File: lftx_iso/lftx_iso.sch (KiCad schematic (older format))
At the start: 9 parts, among them P1 CONN_01X02, P2 CONN_02X08, P3 CONN_02X08, U1 ADUM5402ARWZ

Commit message: moved headers on isolation boards to match actual measurements on lfrx and lftx usrp daughterboards, ready to order
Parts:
- P2: footprint Connect:IDC_Header_Straight_16pins -> Pin_Headers:Pin_Header_Straight_2x08
- P3: footprint Pin_Headers:Pin_Header_Straight_2x08 -> Connect:IDC_Header_Straight_16pins
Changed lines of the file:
@@
 F 0 "P2" H 2400 2800 50  0000 C CNN
 F 1 "CONN_02X08" V 2400 2350 50  0000 C CNN
-F 2 "Connect:IDC_Header_Straight_16pins" H 2400 1150 50  0001 C CNN
+F 2 "Pin_Headers:Pin_Header_Straight_2x08" H 2400 1150 50  0001 C CNN
 F 3 "" H 2400 1150 50  0000 C CNN
 	1    2400 2350
@@
 F 0 "P3" H 9550 2750 50  0000 C CNN
 F 1 "CONN_02X08" V 9550 2300 50  0000 C CNN
-F 2 "Pin_Headers:Pin_Header_Straight_2x08" H 9550 1100 50  0001 C CNN
+F 2 "Connect:IDC_Header_Straight_16pins" H 9550 1100 50  0001 C CNN
 F 3 "" H 9550 1100 50  0000 C CNN
 	1    9550 2300

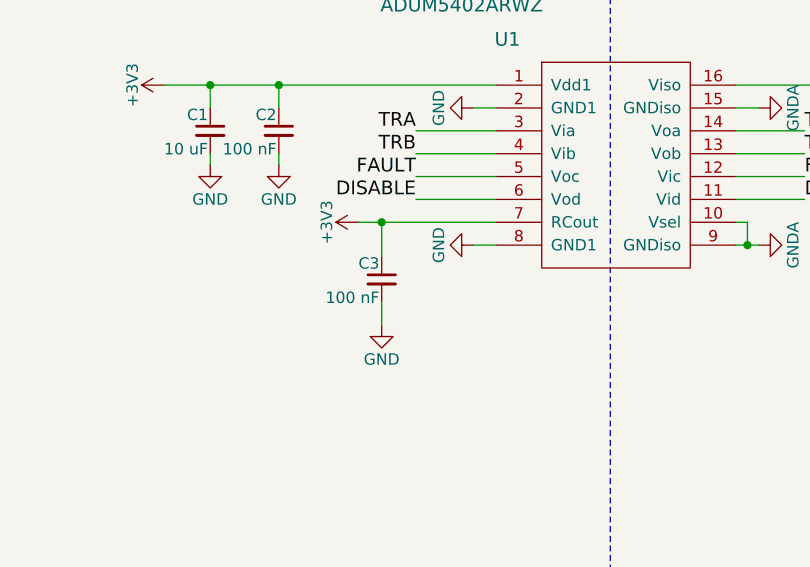
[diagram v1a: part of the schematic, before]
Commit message: added rf-front end module for mcmurdo USRP upgrade
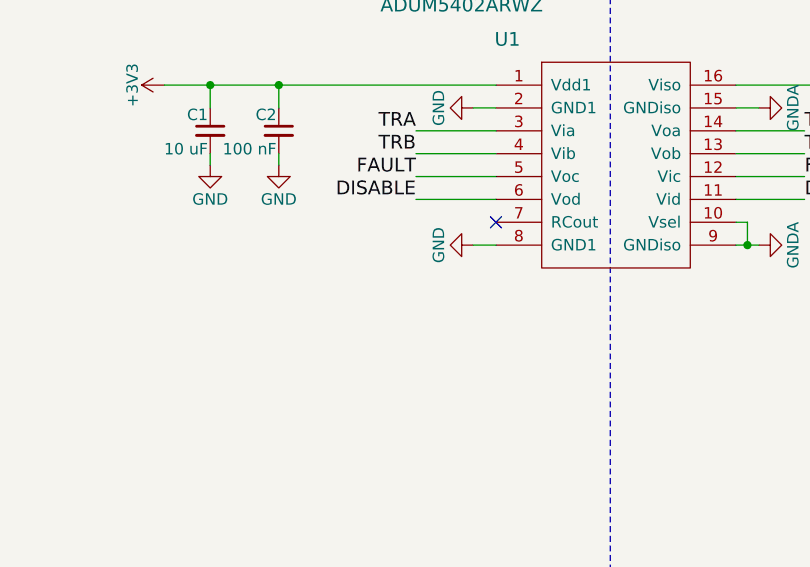
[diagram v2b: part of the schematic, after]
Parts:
- removed C3: 100 nF, Capacitors_SMD:C_0805, symbol C_Small
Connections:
- net +3V3: no longer U1.7 (RCout)
- no-connect marks 8 -> 9
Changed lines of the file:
@@
 	1    0    0    -1
 $EndComp
-$Comp
-L C_Small C3
-U 1 1 59683BA6
-P 4400 4300
-F 0 "C3" H 4410 4370 50  0000 L CNN
-F 1 "100 nF" H 4410 4220 50  0000 L CNN
-F 2 "Capacitors_SMD:C_0805" H 4400 4300 50  0001 C CNN
-F 3 "" H 4400 4300 50  0000 C CNN
-	1    4400 4300
-	-1   0    0    -1
-$EndComp
-$Comp
-L GND #PWR015
-U 1 1 59683BFF
-P 4400 4500
-F 0 "#PWR015" H 4400 4250 50  0001 C CNN
-F 1 "GND" H 4400 4350 50  0000 C CNN
-F 2 "" H 4400 4500 50  0000 C CNN
-F 3 "" H 4400 4500 50  0000 C CNN
-	1    4400 4500
-	1    0    0    -1
-$EndComp
-$Comp
-L +3V3 #PWR016
-U 1 1 59683C25
-P 4300 4050
-F 0 "#PWR016" H 4300 3900 50  0001 C CNN
-F 1 "+3V3" H 4300 4190 50  0000 C CNN
-F 2 "" H 4300 4050 50  0000 C CNN
-F 3 "" H 4300 4050 50  0000 C CNN
-	1    4300 4050
-	0    -1   -1   0
-$EndComp
-Wire Wire Line
-	4300 4050 4900 4050
-Wire Wire Line
-	4400 4050 4400 4200
-Connection ~ 4400 4050
-Wire Wire Line
-	4400 4400 4400 4500
+NoConn ~ 4900 4050
 $EndSCHEMATC
